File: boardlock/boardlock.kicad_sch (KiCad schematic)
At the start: 17 parts, among them U1 ESP32-S3-WROOM-1

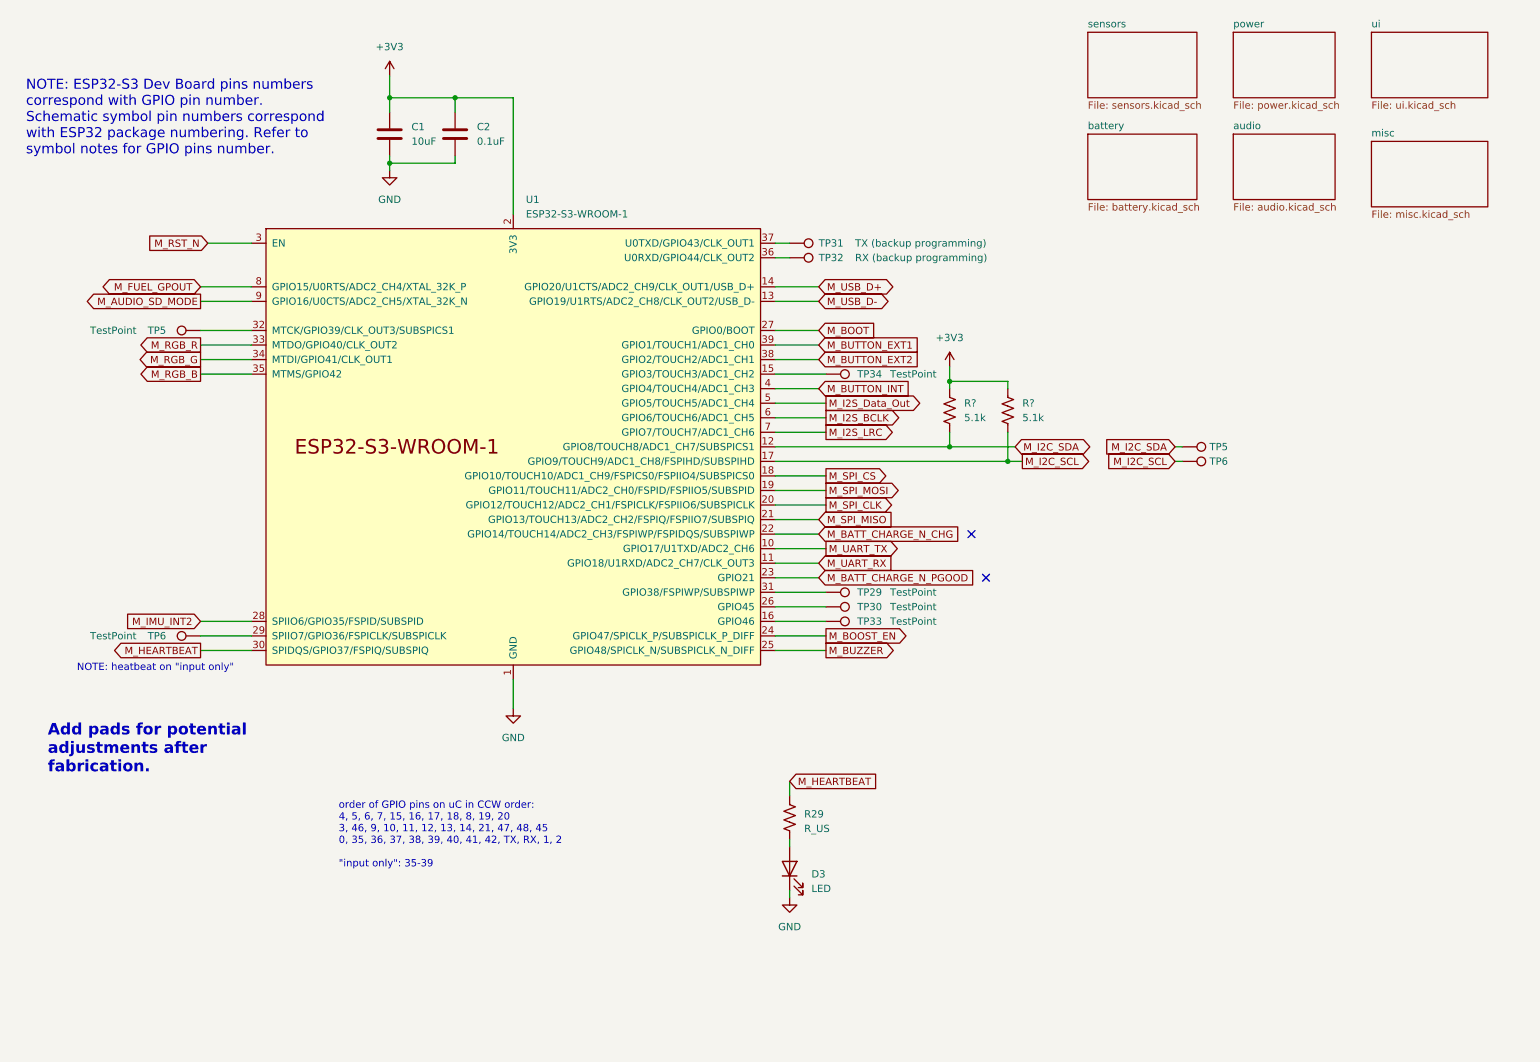
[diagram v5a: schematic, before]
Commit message: delete misc, add testpoints, add sensor signals to micro
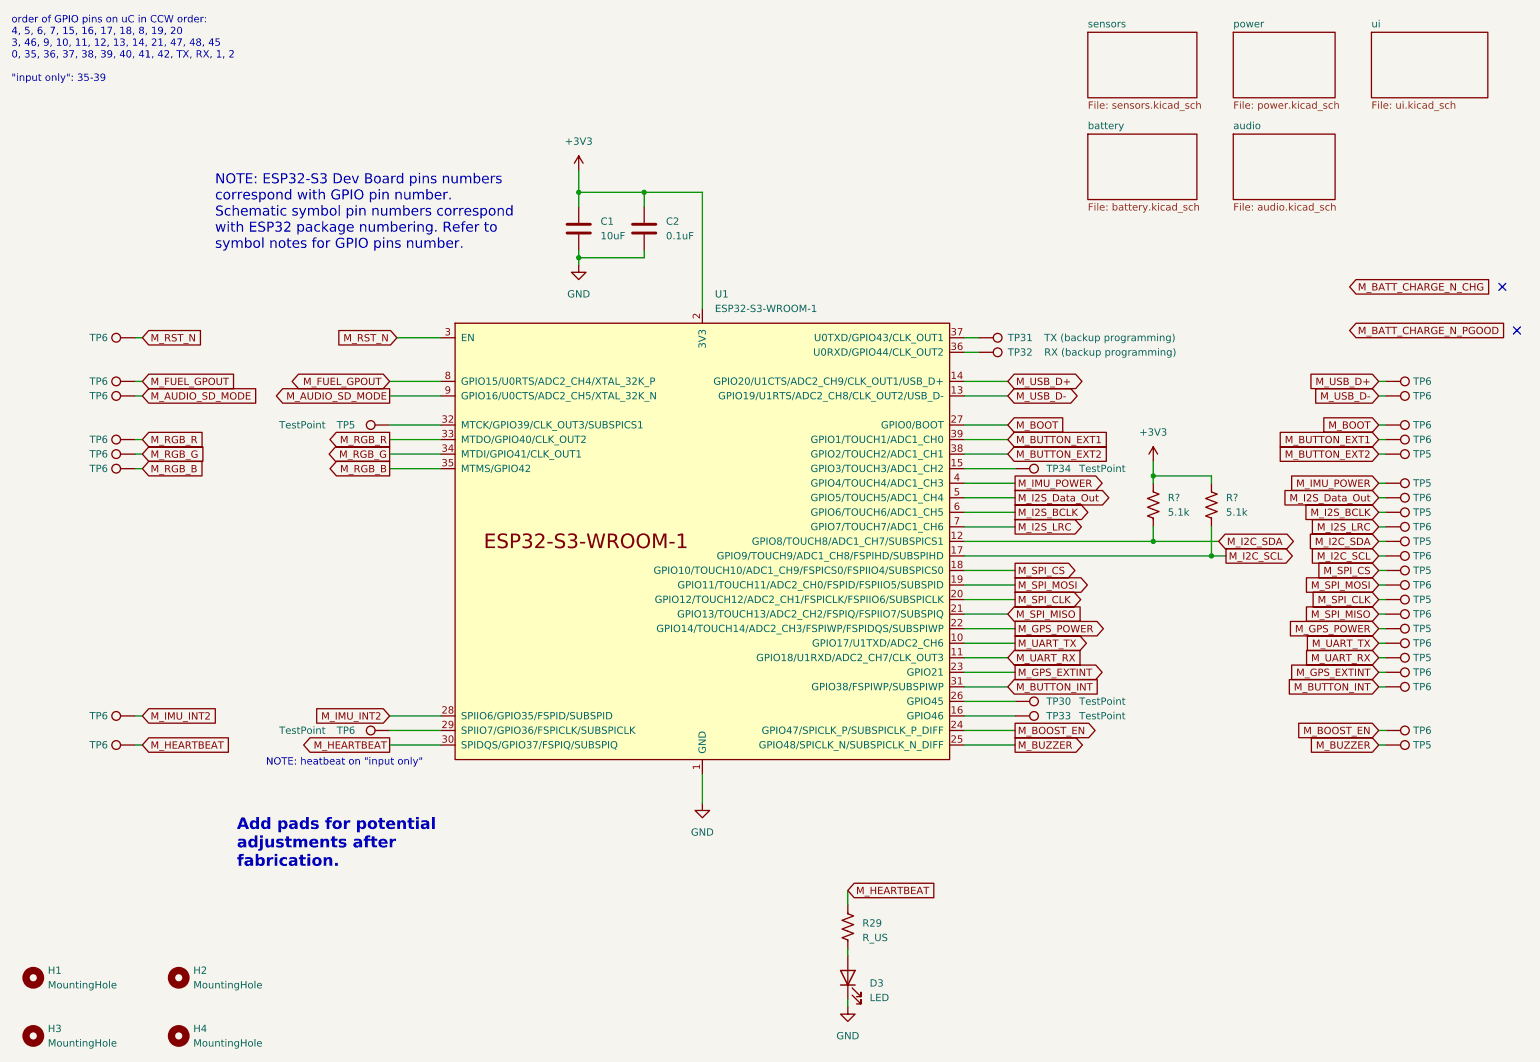
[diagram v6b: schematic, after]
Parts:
- removed TP29: TestPoint, symbol Connector:TestPoint
- added H1, H2, H3, H4: MountingHole, symbol Mechanical:MountingHole
- added TP5 (x8): I2C_SDA, symbol Connector:TestPoint
- added TP6 (x20): I2C_SCL, symbol Connector:TestPoint
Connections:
- net M_AUDIO_SD_MODE: now also TP6.1
- net M_BATT_CHARGE_N_CHG: no longer U1.22 (GPIO14/TOUCH14/ADC2_CH3/FSPIWP/FSPIDQS/SUBSPIWP)
- net M_BATT_CHARGE_N_PGOOD: no longer U1.23 (GPIO21)
- net M_BOOST_EN: now also TP6.1
- net M_BOOT: now also TP6.1
- net M_BUTTON_EXT1: now also TP6.1
- net M_BUTTON_EXT2: now also TP5.1
- net M_BUTTON_INT: now also U1.31 (GPIO38/FSPIWP/SUBSPIWP), TP6.1; no longer U1.4 (GPIO4/TOUCH4/ADC1_CH3)
- net M_BUZZER: now also TP5.1
- net M_FUEL_GPOUT: now also TP6.1
- net M_HEARTBEAT: now also TP6.1
- net M_I2S_BCLK: now also TP5.1
- net M_I2S_Data_Out: now also TP6.1
- net M_I2S_LRC: now also TP6.1
- net M_IMU_INT2: now also TP6.1
- net M_RGB_B: now also TP6.1
- net M_RGB_G: now also TP6.1
- net M_RGB_R: now also TP6.1
- net M_RST_N: now also TP6.1
- net M_SPI_CLK: now also TP5.1
- net M_SPI_CS: now also TP5.1
- net M_SPI_MISO: now also TP6.1
- net M_SPI_MOSI: now also TP6.1
- net M_UART_RX: now also TP5.1
- net M_UART_TX: now also TP6.1
- net M_USB_D+: now also TP6.1
- net M_USB_D-: now also TP6.1
- new net M_GPS_EXTINT: TP6.1, U1.23 (GPIO21)
- new net M_GPS_POWER: TP5.1, U1.22 (GPIO14/TOUCH14/ADC2_CH3/FSPIWP/FSPIDQS/SUBSPIWP)
- new net M_IMU_POWER: TP5.1, U1.4 (GPIO4/TOUCH4/ADC1_CH3)
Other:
- removed sheet misc
- moved on the sheet: C1, C2, D3, R29, R?, TP30, TP31, TP32, TP33, TP34, TP5, TP6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

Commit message: footprint work
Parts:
- C1, C2: footprint (none) -> Capacitor_SMD:C_0805_2012Metric_Pad1.18x1.45mm_HandSolder
- D3: footprint (none) -> LED_SMD:LED_0805_2012Metric_Pad1.15x1.40mm_HandSolder
- R29, R? (x2): footprint (none) -> Resistor_SMD:R_0805_2012Metric_Pad1.20x1.40mm_HandSolder
- TP30, TP31, TP32, TP33, TP34, TP5, TP6: footprint (none) -> TestPoint:TestPoint_Plated_Hole_D3.0mm

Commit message: changes
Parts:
- removed TP5 (x9): I2C_SDA, TestPoint:TestPoint_Plated_Hole_D3.0mm, symbol Connector:TestPoint
- removed TP6 (x21): I2C_SCL, TestPoint:TestPoint_Plated_Hole_D3.0mm, symbol Connector:TestPoint
- added TP10, TP11, TP12, TP13, TP14, TP15, TP16, TP17, TP18, TP19, TP20, TP22, TP23, TP24, TP25, TP26, TP27, TP28, TP29, TP35, TP36, TP37, TP38, TP39, TP4, TP41, TP42, TP7, TP8, TP9: TestPoint, symbol Connector:TestPoint
- TP31: value TX (backup programming) -> TestPoint; footprint TestPoint:TestPoint_Plated_Hole_D3.0mm -> (none)
- TP32: value RX (backup programming) -> TestPoint; footprint TestPoint:TestPoint_Plated_Hole_D3.0mm -> (none)
- TP6: footprint TestPoint:TestPoint_Plated_Hole_D3.0mm -> TestPoint:TestPoint_Pad_D1.0mm
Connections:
- net M_AUDIO_SD_MODE: now also TP13.1
- net M_BOOST_EN: now also TP41.1
- net M_BOOT: now also TP8.1
- net M_BUTTON_EXT1: now also TP17.1
- net M_BUTTON_EXT2: now also TP18.1
- net M_BUTTON_INT: now also TP39.1
- net M_BUZZER: now also TP42.1
- net M_FUEL_GPOUT: now also TP14.1
- net M_GPS_EXTINT: now also TP38.1
- net M_GPS_POWER: now also TP35.1
- net M_HEARTBEAT: now also TP15.1
- net M_I2C_SCL: now also TP25.1
- net M_I2C_SDA: now also TP24.1
- net M_I2S_BCLK: now also TP22.1
- net M_I2S_Data_Out: now also TP20.1
- net M_I2S_LRC: now also TP23.1
- net M_IMU_INT2: now also TP9.1
- net M_IMU_POWER: now also TP19.1
- net M_RGB_B: now also TP10.1
- net M_RGB_G: now also TP11.1
- net M_RGB_R: now also TP12.1
- net M_RST_N: now also TP16.1
- net M_SPI_CLK: now also TP28.1
- net M_SPI_CS: now also TP26.1
- net M_SPI_MISO: now also TP29.1
- net M_SPI_MOSI: now also TP27.1
- net M_UART_RX: now also TP37.1
- net M_UART_TX: now also TP36.1
- net M_USB_D+: now also TP4.1
- net M_USB_D-: now also TP7.1
